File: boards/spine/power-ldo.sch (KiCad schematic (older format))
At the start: 6 parts

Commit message: Power management and such
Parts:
- gave numbers to parts that had none: 6
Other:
- moved on the sheet: C74, C75, C76, C77, U13, U14

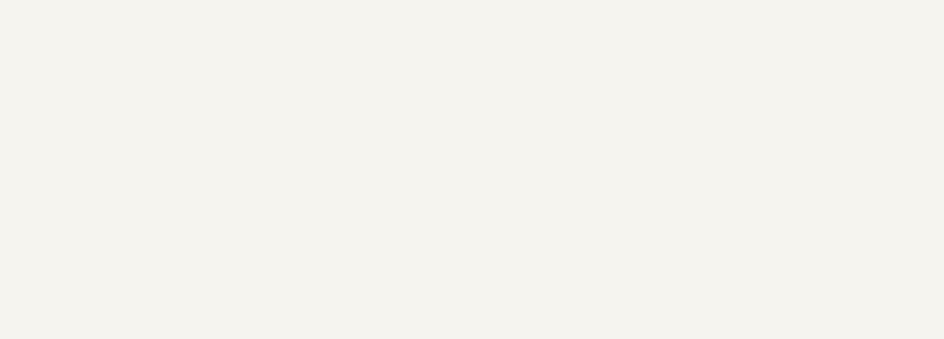
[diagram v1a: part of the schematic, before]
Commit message: Clock generator, sync connectors, title blocks
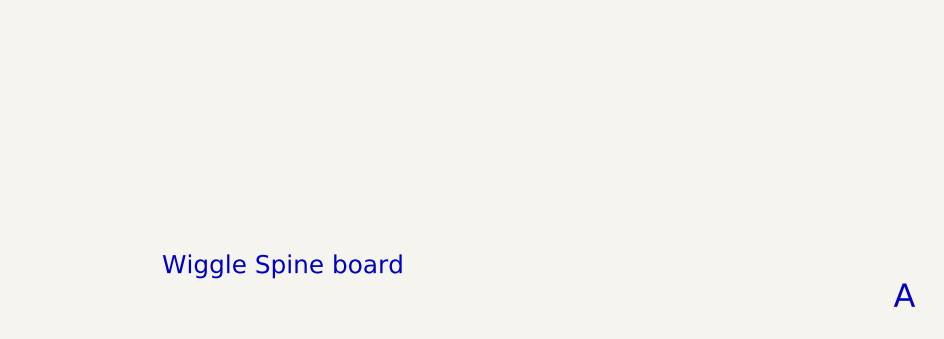
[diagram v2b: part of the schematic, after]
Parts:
- C74, C75, C76, C77: footprint 0805 -> Capacitors_SMD:C_0805
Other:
- note added: "A"
- note added: "Wiggle Spine board"

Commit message: Schematic footprint and refdes work
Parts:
- U13: footprint SOT-753 -> TO_SOT_Packages_SMD:SOT-353; MfgId TCR2EF25,LM(CT -> TCR2EF25.LM(CT
- U14: footprint SOT-753 -> TO_SOT_Packages_SMD:SOT-353; MfgId TCR2EF12,LM(CT -> TCR2EF12.LM(CT
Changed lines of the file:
@@
 F 0 "U14" H 6750 4550 60  0000 L CNN
 F 1 "TCR2EF12" H 6750 3950 60  0000 L CNN
-F 2 "SOT-753" H 7000 4550 60  0001 C CNN
+F 2 "TO_SOT_Packages_SMD:SOT-353" H 7000 4550 60  0001 C CNN
 F 3 "http://www.semicon.toshiba.co.jp/info/docget.jsp?pid=TCR2EE10&lang=en&type=datasheet" H 7000 4550 60  0001 C CNN
 F 4 "TCR2EF12LM(CTCT-ND" H 7100 4400 60  0001 C CNN "Vend1Id"
 F 5 "Digikey" H 7100 4400 60  0001 C CNN "Vend1"
 F 6 "Toshiba" H 7100 4400 60  0001 C CNN "MfrId"
-F 7 "TCR2EF12,LM(CT" H 7100 4400 60  0001 C CNN "MfgId"
+F 7 "TCR2EF12.LM(CT" H 7100 4400 60  0001 C CNN "MfgId"
 F 8 "LDO 1.2V 200mA" H 7000 3850 39  0000 C CNN "Description"
 F 9 "0.07110" H 7100 4400 60  0001 C CNN "RefPrice1k"
@@
 $EndComp
 $Comp
-L GND #PWR0143
+L GND #PWR149
 U 1 1 564D1EB9
 P 7850 4950
-F 0 "#PWR0143" H 7850 4700 50  0001 C CNN
+F 0 "#PWR149" H 7850 4700 50  0001 C CNN
 F 1 "GND" H 7850 4800 50  0000 C CNN
 F 2 "" H 7850 4950 60  0000 C CNN
@@
 NoConn ~ 7650 4550
 $Comp
-L GND #PWR0144
+L GND #PWR147
 U 1 1 564D1EBA
 P 6150 5000
-F 0 "#PWR0144" H 6150 4750 50  0001 C CNN
+F 0 "#PWR147" H 6150 4750 50  0001 C CNN
 F 1 "GND" H 6150 4850 50  0000 C CNN
 F 2 "" H 6150 5000 60  0000 C CNN
@@
 F 0 "U13" H 4050 4550 60  0000 L CNN
 F 1 "TCR2EF25" H 4050 3950 60  0000 L CNN
-F 2 "SOT-753" H 4300 4550 60  0001 C CNN
+F 2 "TO_SOT_Packages_SMD:SOT-353" H 4300 4550 60  0001 C CNN
 F 3 "http://www.semicon.toshiba.co.jp/info/docget.jsp?pid=TCR2EE10&lang=en&type=datasheet" H 4300 4550 60  0001 C CNN
 F 4 "TCR2EF25LM(CTCT-ND" H 4400 4400 60  0001 C CNN "Vend1Id"
 F 5 "Digikey" H 4400 4400 60  0001 C CNN "Vend1"
 F 6 "Toshiba" H 4400 4400 60  0001 C CNN "MfrId"
-F 7 "TCR2EF25,LM(CT" H 4400 4400 60  0001 C CNN "MfgId"
+F 7 "TCR2EF25.LM(CT" H 4400 4400 60  0001 C CNN "MfgId"
 F 8 "LDO 2.5V 200mA" H 4300 3850 39  0000 C CNN "Description"
 F 9 "0.07110" H 4400 4400 60  0001 C CNN "RefPrice1k"
@@
 $EndComp
 $Comp
-L GND #PWR0145
+L GND #PWR146
 U 1 1 564D1EBE
 P 5150 4950
-F 0 "#PWR0145" H 5150 4700 50  0001 C CNN
+F 0 "#PWR146" H 5150 4700 50  0001 C CNN
 F 1 "GND" H 5150 4800 50  0000 C CNN
 F 2 "" H 5150 4950 60  0000 C CNN
@@
 NoConn ~ 4950 4550
 $Comp
-L GND #PWR0146
+L GND #PWR144
 U 1 1 564D1EBF
 P 3450 5000
-F 0 "#PWR0146" H 3450 4750 50  0001 C CNN
+F 0 "#PWR144" H 3450 4750 50  0001 C CNN
 F 1 "GND" H 3450 4850 50  0000 C CNN
 F 2 "" H 3450 5000 60  0000 C CNN
@@
 $EndComp
 $Comp
-L +2V5 #PWR0147
+L +2V5 #PWR145
 U 1 1 564D1EC0
 P 5150 4300
-F 0 "#PWR0147" H 5150 4150 50  0001 C CNN
+F 0 "#PWR145" H 5150 4150 50  0001 C CNN
 F 1 "+2V5" H 5150 4440 50  0000 C CNN
 F 2 "" H 5150 4300 60  0000 C CNN
@@
 2.5v = FPGA NVCM programming voltage\n\n(Some circuits approximate this with a diode\ndrop from 3.3v, but that's pretty dirty and\nthese LDOs are about as cheap as a diode.)
 $Comp
-L +3.3V #PWR0148
+L +3.3V #PWR143
 U 1 1 564D1EC2
 P 3450 4300
-F 0 "#PWR0148" H 3450 4150 50  0001 C CNN
+F 0 "#PWR143" H 3450 4150 50  0001 C CNN
 F 1 "+3.3V" H 3450 4440 50  0000 C CNN
 F 2 "" H 3450 4300 60  0000 C CNN
@@
 $EndComp
 $Comp
-L +1V2 #PWR0149
+L +1V2 #PWR148
 U 1 1 564D1EC3
 P 7850 4300
-F 0 "#PWR0149" H 7850 4150 50  0001 C CNN
+F 0 "#PWR148" H 7850 4150 50  0001 C CNN
 F 1 "+1V2" H 7850 4440 50  0000 C CNN
 F 2 "" H 7850 4300 60  0000 C CNN

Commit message: Fix some 6-pin packages
I had several of these mislabeled as SOT23-6, but there are no SOT23-6 parts here. The LDOs are SOT23-5, and the others (TVS diode array and inverters) are in the smaller SC-88 package.
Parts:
- U13, U14: footprint TO_SOT_Packages_SMD:SOT-353 -> TO_SOT_Packages_SMD:SOT-23-5
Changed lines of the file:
@@
 F 0 "U14" H 6750 4550 60  0000 L CNN
 F 1 "TCR2EF12" H 6750 3950 60  0000 L CNN
-F 2 "TO_SOT_Packages_SMD:SOT-353" H 7000 4550 60  0001 C CNN
+F 2 "TO_SOT_Packages_SMD:SOT-23-5" H 7000 4550 60  0001 C CNN
 F 3 "http://www.semicon.toshiba.co.jp/info/docget.jsp?pid=TCR2EE10&lang=en&type=datasheet" H 7000 4550 60  0001 C CNN
 F 4 "TCR2EF12LM(CTCT-ND" H 7100 4400 60  0001 C CNN "Vend1Id"
@@
 $EndComp
 $Comp
-L GND #PWR151
+L GND #PWR0145
 U 1 1 564D1EB9
 P 7850 4950
-F 0 "#PWR151" H 7850 4700 50  0001 C CNN
+F 0 "#PWR0145" H 7850 4700 50  0001 C CNN
 F 1 "GND" H 7850 4800 50  0000 C CNN
 F 2 "" H 7850 4950 60  0000 C CNN
@@
 NoConn ~ 7650 4550
 $Comp
-L GND #PWR149
+L GND #PWR0146
 U 1 1 564D1EBA
 P 6150 5000
-F 0 "#PWR149" H 6150 4750 50  0001 C CNN
+F 0 "#PWR0146" H 6150 4750 50  0001 C CNN
 F 1 "GND" H 6150 4850 50  0000 C CNN
 F 2 "" H 6150 5000 60  0000 C CNN
@@
 F 0 "U13" H 4050 4550 60  0000 L CNN
 F 1 "TCR2EF25" H 4050 3950 60  0000 L CNN
-F 2 "TO_SOT_Packages_SMD:SOT-353" H 4300 4550 60  0001 C CNN
+F 2 "TO_SOT_Packages_SMD:SOT-23-5" H 4300 4550 60  0001 C CNN
 F 3 "http://www.semicon.toshiba.co.jp/info/docget.jsp?pid=TCR2EE10&lang=en&type=datasheet" H 4300 4550 60  0001 C CNN
 F 4 "TCR2EF25LM(CTCT-ND" H 4400 4400 60  0001 C CNN "Vend1Id"
@@
 $EndComp
 $Comp
-L GND #PWR148
+L GND #PWR0147
 U 1 1 564D1EBE
 P 5150 4950
-F 0 "#PWR148" H 5150 4700 50  0001 C CNN
+F 0 "#PWR0147" H 5150 4700 50  0001 C CNN
 F 1 "GND" H 5150 4800 50  0000 C CNN
 F 2 "" H 5150 4950 60  0000 C CNN
@@
 NoConn ~ 4950 4550
 $Comp
-L GND #PWR146
+L GND #PWR0148
 U 1 1 564D1EBF
 P 3450 5000
-F 0 "#PWR146" H 3450 4750 50  0001 C CNN
+F 0 "#PWR0148" H 3450 4750 50  0001 C CNN
 F 1 "GND" H 3450 4850 50  0000 C CNN
 F 2 "" H 3450 5000 60  0000 C CNN
@@
 $EndComp
 $Comp
-L +2V5 #PWR147
+L +2V5 #PWR0149
 U 1 1 564D1EC0
 P 5150 4300
-F 0 "#PWR147" H 5150 4150 50  0001 C CNN
+F 0 "#PWR0149" H 5150 4150 50  0001 C CNN
 F 1 "+2V5" H 5150 4440 50  0000 C CNN
 F 2 "" H 5150 4300 60  0000 C CNN
@@
 2.5v = FPGA NVCM programming voltage\n\n(Some circuits approximate this with a diode\ndrop from 3.3v, but that's pretty dirty and\nthese LDOs are about as cheap as a diode.)
 $Comp
-L +3.3V #PWR145
+L +3.3V #PWR0150
 U 1 1 564D1EC2
 P 3450 4300
-F 0 "#PWR145" H 3450 4150 50  0001 C CNN
+F 0 "#PWR0150" H 3450 4150 50  0001 C CNN
 F 1 "+3.3V" H 3450 4440 50  0000 C CNN
 F 2 "" H 3450 4300 60  0000 C CNN
@@
 $EndComp
 $Comp
-L +1V2 #PWR150
+L +1V2 #PWR0151
 U 1 1 564D1EC3
 P 7850 4300
-F 0 "#PWR150" H 7850 4150 50  0001 C CNN
+F 0 "#PWR0151" H 7850 4150 50  0001 C CNN
 F 1 "+1V2" H 7850 4440 50  0000 C CNN
 F 2 "" H 7850 4300 60  0000 C CNN
@@
 FB 59 00 E6 A5 69 3A 37 9E CF 73 BC F7 37 E3 33 5D 9E A8 3E 7F 80 FA F7 F6 BB 44 F4 6E D4 E7 77
 A2 1E 1F 27 A2 E3 16 70 32 E9 54 FE 3F E7 AF 00 CA 1C A3 36 0A 00 00 00 00 49 45 4E 44 AE 42 60
-82 FF
+82 00
 EndData
 $EndBitmap
@@
 72 0F 1C A9 DC 70 49 CB 79 33 88 85 99 AD 01 6C 4B 10 FC 3B 13 DE 3B 37 68 79 AD 07 BC 00 3C 0E
 3C 31 EE E3 D8 E7 0F 03 D7 7B 9F FB C1 E1 FF 01 18 C4 96 1D B8 0E 40 07 00 00 00 00 49 45 4E 44
-AE 42 60 82 A3
+AE 42 60 82 00
 EndData
 $EndBitmap
